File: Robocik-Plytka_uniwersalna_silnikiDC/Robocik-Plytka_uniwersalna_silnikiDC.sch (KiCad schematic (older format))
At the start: 67 parts, among them IC1 ACSL-6400-00TE, IC2 L6205D, J1 Conn_01x03, J2 Conn_01x02, J3 Conn_01x04, J4 Conn_01x02, J5 Conn_01x03, J6 Conn_01x02, Q1 BC847, Q2 BC847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

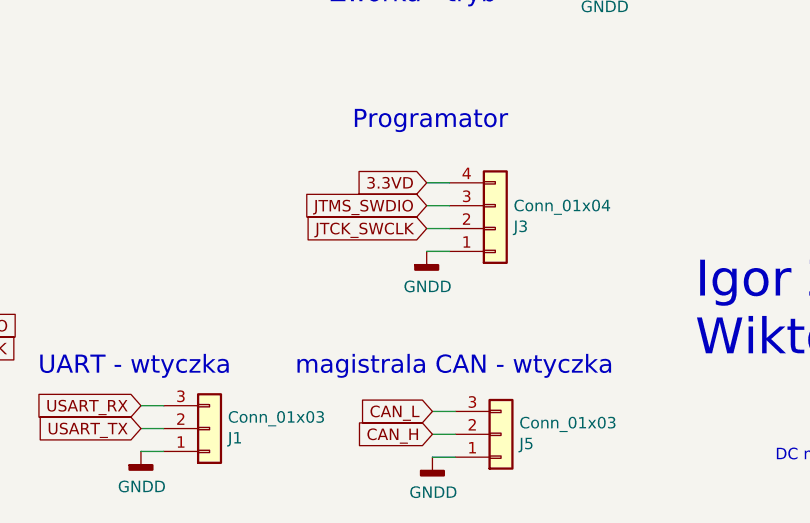
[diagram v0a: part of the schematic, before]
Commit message: Moved all connectors to the same side of PCB. Redesigned ground planes. Added folder "quick view" which consists of PCB schematic, layout, jpegs of PCB top and bottom side and new added step 3D model.
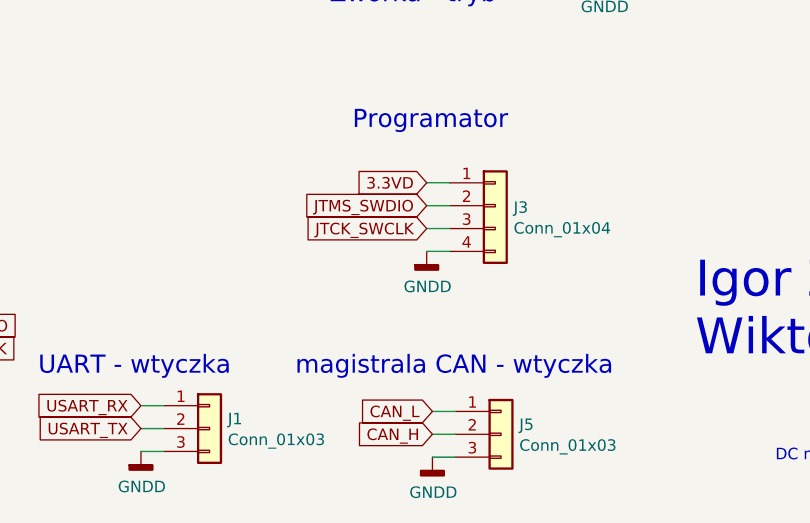
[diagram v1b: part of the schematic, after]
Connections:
- net 3.3VD: now also J3.1 (Pin_1); no longer J3.4 (Pin_4)
- net CAN_L: now also J5.1 (Pin_1); no longer J5.3 (Pin_3)
- net GNDD: now also J1.3 (Pin_3), J3.4 (Pin_4), J5.3 (Pin_3); no longer J1.1 (Pin_1), J3.1 (Pin_1), J5.1 (Pin_1)
- net JTCK_SWCLK: now also J3.3 (Pin_3); no longer J3.2 (Pin_2)
- net JTMS_SWDIO: now also J3.2 (Pin_2); no longer J3.3 (Pin_3)
- net USART_RX: now also J1.1 (Pin_1); no longer J1.3 (Pin_3)
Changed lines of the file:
@@
 L Connector_Generic:Conn_01x04 J3
 U 1 1 5E5A9771
-P 6225 6475
-F 0 "J3" H 6305 6467 50  0000 L CNN
-F 1 "Conn_01x04" H 6305 6376 50  0000 L CNN
-F 2 "22-05-7045:22-05-7045" H 6225 6475 50  0001 C CNN
-F 3 "~" H 6225 6475 50  0001 C CNN
-	1    6225 6475
-	1    0    0    1
+P 6225 6375
+F 0 "J3" H 6305 6367 50  0000 L CNN
+F 1 "Conn_01x04" H 6305 6276 50  0000 L CNN
+F 2 "22-05-7045:22-05-7045" H 6225 6375 50  0001 C CNN
+F 3 "~" H 6225 6375 50  0001 C CNN
+	1    6225 6375
+	1    0    0    -1
 $EndComp
 $Comp
@@
 F 3 "~" H 6250 7375 50  0001 C CNN
 	1    6250 7375
-	1    0    0    1
+	1    0    0    -1
 $EndComp
 $Comp
@@
 F 3 "~" H 4975 7350 50  0001 C CNN
 	1    4975 7350
-	1    0    0    1
+	1    0    0    -1
 $EndComp
 Wire Wire Line

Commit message: Added missing 3D model for optocoupler. Moved all connector to the other side of the board. Reduced PCB size.
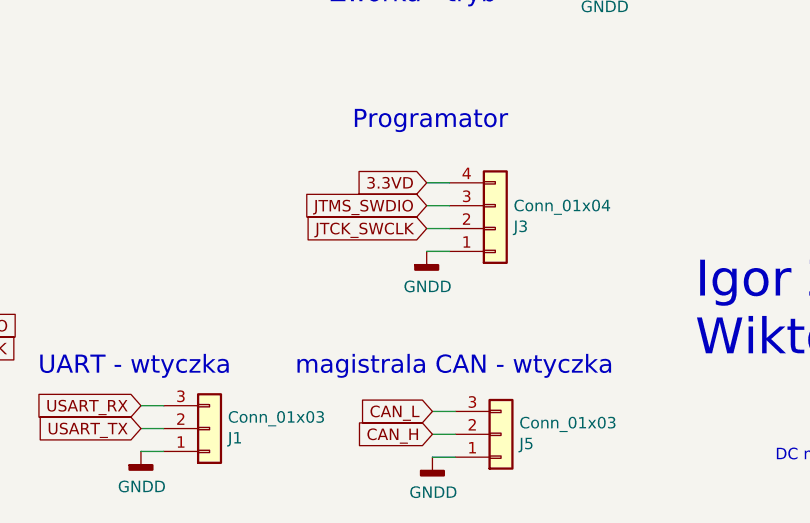
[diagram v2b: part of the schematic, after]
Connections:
- net 3.3VD: now also J3.4 (Pin_4); no longer J3.1 (Pin_1)
- net CAN_L: now also J5.3 (Pin_3); no longer J5.1 (Pin_1)
- net GNDD: now also J1.1 (Pin_1), J3.1 (Pin_1), J5.1 (Pin_1); no longer J1.3 (Pin_3), J3.4 (Pin_4), J5.3 (Pin_3)
- net JTCK_SWCLK: now also J3.2 (Pin_2); no longer J3.3 (Pin_3)
- net JTMS_SWDIO: now also J3.3 (Pin_3); no longer J3.2 (Pin_2)
- net USART_RX: now also J1.3 (Pin_3); no longer J1.1 (Pin_1)
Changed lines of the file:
@@
 EESchema Schematic File Version 4
-LIBS:Robocik-Plytka_uniwersalna_silnikiDC-cache
 EELAYER 29 0
 EELAYER END
@@
 Wire Wire Line
 	4675 7350 4775 7350
-Wire Wire Line
-	6025 6275 5925 6275
-Wire Wire Line
-	5925 6375 6025 6375
-Wire Wire Line
-	6025 6475 5925 6475
-Wire Wire Line
-	5925 6575 6025 6575
 Text GLabel 7950 4200 2    50   Input ~ 0
 CAN_H
@@
 	5950 7475 6050 7475
 $Comp
-L Connector_Generic:Conn_01x04 J3
-U 1 1 5E5A9771
-P 6225 6375
-F 0 "J3" H 6305 6367 50  0000 L CNN
-F 1 "Conn_01x04" H 6305 6276 50  0000 L CNN
-F 2 "22-05-7045:22-05-7045" H 6225 6375 50  0001 C CNN
-F 3 "~" H 6225 6375 50  0001 C CNN
-	1    6225 6375
-	1    0    0    -1
-$EndComp
-$Comp
 L Connector_Generic:Conn_01x03 J5
 U 1 1 5E5AA71E
@@
 F 3 "~" H 6250 7375 50  0001 C CNN
 	1    6250 7375
-	1    0    0    -1
+	1    0    0    1
 $EndComp
 $Comp
@@
 F 3 "~" H 4975 7350 50  0001 C CNN
 	1    4975 7350
-	1    0    0    -1
+	1    0    0    1
 $EndComp
 Wire Wire Line
@@
 Text Notes 7750 5450 0    79   ~ 0
 Zasilanie - wtyczki
+Wire Wire Line
+	5925 6575 6025 6575
+Wire Wire Line
+	6025 6475 5925 6475
+Wire Wire Line
+	5925 6375 6025 6375
+Wire Wire Line
+	6025 6275 5925 6275
+$Comp
+L Connector_Generic:Conn_01x04 J3
+U 1 1 5E5A9771
+P 6225 6475
+F 0 "J3" H 6305 6467 50  0000 L CNN
+F 1 "Conn_01x04" H 6305 6376 50  0000 L CNN
+F 2 "22-05-7045:22-05-7045" H 6225 6475 50  0001 C CNN
+F 3 "~" H 6225 6475 50  0001 C CNN
+	1    6225 6475
+	1    0    0    1
+$EndComp
 $EndSCHEMATC

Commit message: Fixed size of LSE crystal oscilator. Added 3D models for LSE and HSE oscilators.
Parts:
- Y2: footprint Crystal:Crystal_SMD_5032-2Pin_5.0x3.2mm -> Crystal:Crystal_SMD_3215-2Pin_3.2x1.5mm
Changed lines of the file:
@@
 EESchema Schematic File Version 4
+LIBS:Robocik-Plytka_uniwersalna_silnikiDC-cache
 EELAYER 29 0
 EELAYER END
@@
 F 0 "Y2" V 1896 5262 50  0000 R CNN
 F 1 "LSE OSC" V 1700 5450 50  0000 R CNN
-F 2 "Crystal:Crystal_SMD_5032-2Pin_5.0x3.2mm" H 1850 5350 50  0001 C CNN
+F 2 "Crystal:Crystal_SMD_3215-2Pin_3.2x1.5mm" H 1850 5350 50  0001 C CNN
 F 3 "~" H 1850 5350 50  0001 C CNN
 	1    1850 5350

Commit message: Added capacitors values for crystals. Redesigned low-pass filters at EN pins of driver: changed R and C values.
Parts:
- C16, C17: value 5.6nF -> 10nF
- C2, C3: value 100nF -> 27pF
- C4, C5: value 100nF -> 8.2pF
- IC1: symbol ACSL-6400-00TE:ACSL-6400-00TE -> Robocik-Plytka_uniwersalna_silnikiDC-rescue:ACSL-6400-00TE-ACSL-6400-00TE
- IC2: symbol L6205D:L6205D -> Robocik-Plytka_uniwersalna_silnikiDC-rescue:L6205D-L6205D
- R19, R20: value 100k -> 56k
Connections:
- net GNDA: now also IC1.9 (GND_1)
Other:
- note added: "09.03.2020"
- note removed: "23.02.2020"
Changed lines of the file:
@@
 EESchema Schematic File Version 4
-LIBS:Robocik-Plytka_uniwersalna_silnikiDC-cache
-EELAYER 29 0
+EELAYER 30 0
 EELAYER END
 $Descr A4 11693 8268
@@
 $EndDescr
 $Comp
-L ACSL-6400-00TE:ACSL-6400-00TE IC1
+L Robocik-Plytka_uniwersalna_silnikiDC-rescue:ACSL-6400-00TE-ACSL-6400-00TE IC1
 U 1 1 5E4442A1
 P 2950 1850
@@
 P 9400 2250
 F 0 "R19" V 9204 2250 50  0000 C CNN
-F 1 "100k" V 9295 2250 50  0000 C CNN
+F 1 "56k" V 9295 2250 50  0000 C CNN
 F 2 "Resistor_SMD:R_0805_2012Metric" H 9400 2250 50  0001 C CNN
 F 3 "~" H 9400 2250 50  0001 C CNN
@@
 P 9650 1000
 F 0 "R20" V 9846 1000 50  0000 C CNN
-F 1 "100k" V 9755 1000 50  0000 C CNN
+F 1 "56k" V 9755 1000 50  0000 C CNN
 F 2 "Resistor_SMD:R_0805_2012Metric" H 9650 1000 50  0001 C CNN
 F 3 "~" H 9650 1000 50  0001 C CNN
@@
 P 9250 2400
 F 0 "C16" H 9342 2446 50  0000 L CNN
-F 1 "5.6nF" H 9342 2355 50  0000 L CNN
+F 1 "10nF" H 9342 2355 50  0000 L CNN
 F 2 "Capacitor_SMD:C_0805_2012Metric" H 9250 2400 50  0001 C CNN
 F 3 "~" H 9250 2400 50  0001 C CNN
@@
 P 9450 1150
 F 0 "C17" H 9542 1196 50  0000 L CNN
-F 1 "5.6nF" H 9542 1105 50  0000 L CNN
+F 1 "10nF" H 9542 1105 50  0000 L CNN
 F 2 "Capacitor_SMD:C_0805_2012Metric" H 9450 1150 50  0001 C CNN
 F 3 "~" H 9450 1150 50  0001 C CNN
@@
 P 1650 4850
 F 0 "C2" H 1650 4950 50  0000 L CNN
-F 1 "100nF" H 1750 4850 50  0000 L CNN
+F 1 "27pF" H 1750 4850 50  0000 L CNN
 F 2 "Capacitor_SMD:C_0805_2012Metric" H 1650 4850 50  0001 C CNN
 F 3 "~" H 1650 4850 50  0001 C CNN
@@
 P 1650 5050
 F 0 "C3" H 1700 5150 50  0000 L CNN
-F 1 "100nF" H 1600 5000 50  0000 L CNN
+F 1 "27pF" H 1600 5000 50  0000 L CNN
 F 2 "Capacitor_SMD:C_0805_2012Metric" H 1650 5050 50  0001 C CNN
 F 3 "~" H 1650 5050 50  0001 C CNN
@@
 P 1650 5250
 F 0 "C4" H 1550 5350 50  0000 L CNN
-F 1 "100nF" H 1650 5350 50  0000 L CNN
+F 1 "8.2pF" H 1650 5350 50  0000 L CNN
 F 2 "Capacitor_SMD:C_0805_2012Metric" H 1650 5250 50  0001 C CNN
 F 3 "~" H 1650 5250 50  0001 C CNN
@@
 P 1650 5450
 F 0 "C5" H 1550 5550 50  0000 L CNN
-F 1 "100nF" H 1600 5400 50  0000 L CNN
+F 1 "8.2pF" H 1600 5400 50  0000 L CNN
 F 2 "Capacitor_SMD:C_0805_2012Metric" H 1650 5450 50  0001 C CNN
 F 3 "~" H 1650 5450 50  0001 C CNN
@@
 $EndComp
 Text Notes 8300 7650 0    50   ~ 0
-23.02.2020
+09.03.2020
 NoConn ~ 2250 7100
 NoConn ~ 2250 7000
@@
 	9250 2050 9200 2050
 $Comp
-L L6205D:L6205D IC2
+L Robocik-Plytka_uniwersalna_silnikiDC-rescue:L6205D-L6205D IC2
 U 1 1 5E44D3C3
 P 7900 1350
@@
 	1    0    0    1
 $EndComp
+$Comp
+L power:GNDA #PWR?
+U 1 1 5E679B20
+P 4350 2550
+F 0 "#PWR?" H 4350 2300 50  0001 C CNN
+F 1 "GNDA" H 4355 2377 50  0001 C CNN
+F 2 "" H 4350 2550 50  0001 C CNN
+F 3 "" H 4350 2550 50  0001 C CNN
+	1    4350 2550
+	1    0    0    -1
+$EndComp
 $EndSCHEMATC
